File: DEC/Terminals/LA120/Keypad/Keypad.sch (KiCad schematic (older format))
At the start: 23 parts, among them J1 TO KEYBOARD, SW1 ENTER, SW10 9, SW11 0, SW12 COMMA, SW13 MINUS, SW14 PF1, SW15 PF2, SW16 PF3, SW17 PF4, SW18 PERIOD, SW2 1, SW3 2, SW4 3, SW5 4, SW6 5, SW7 6, SW8 7, SW9 8

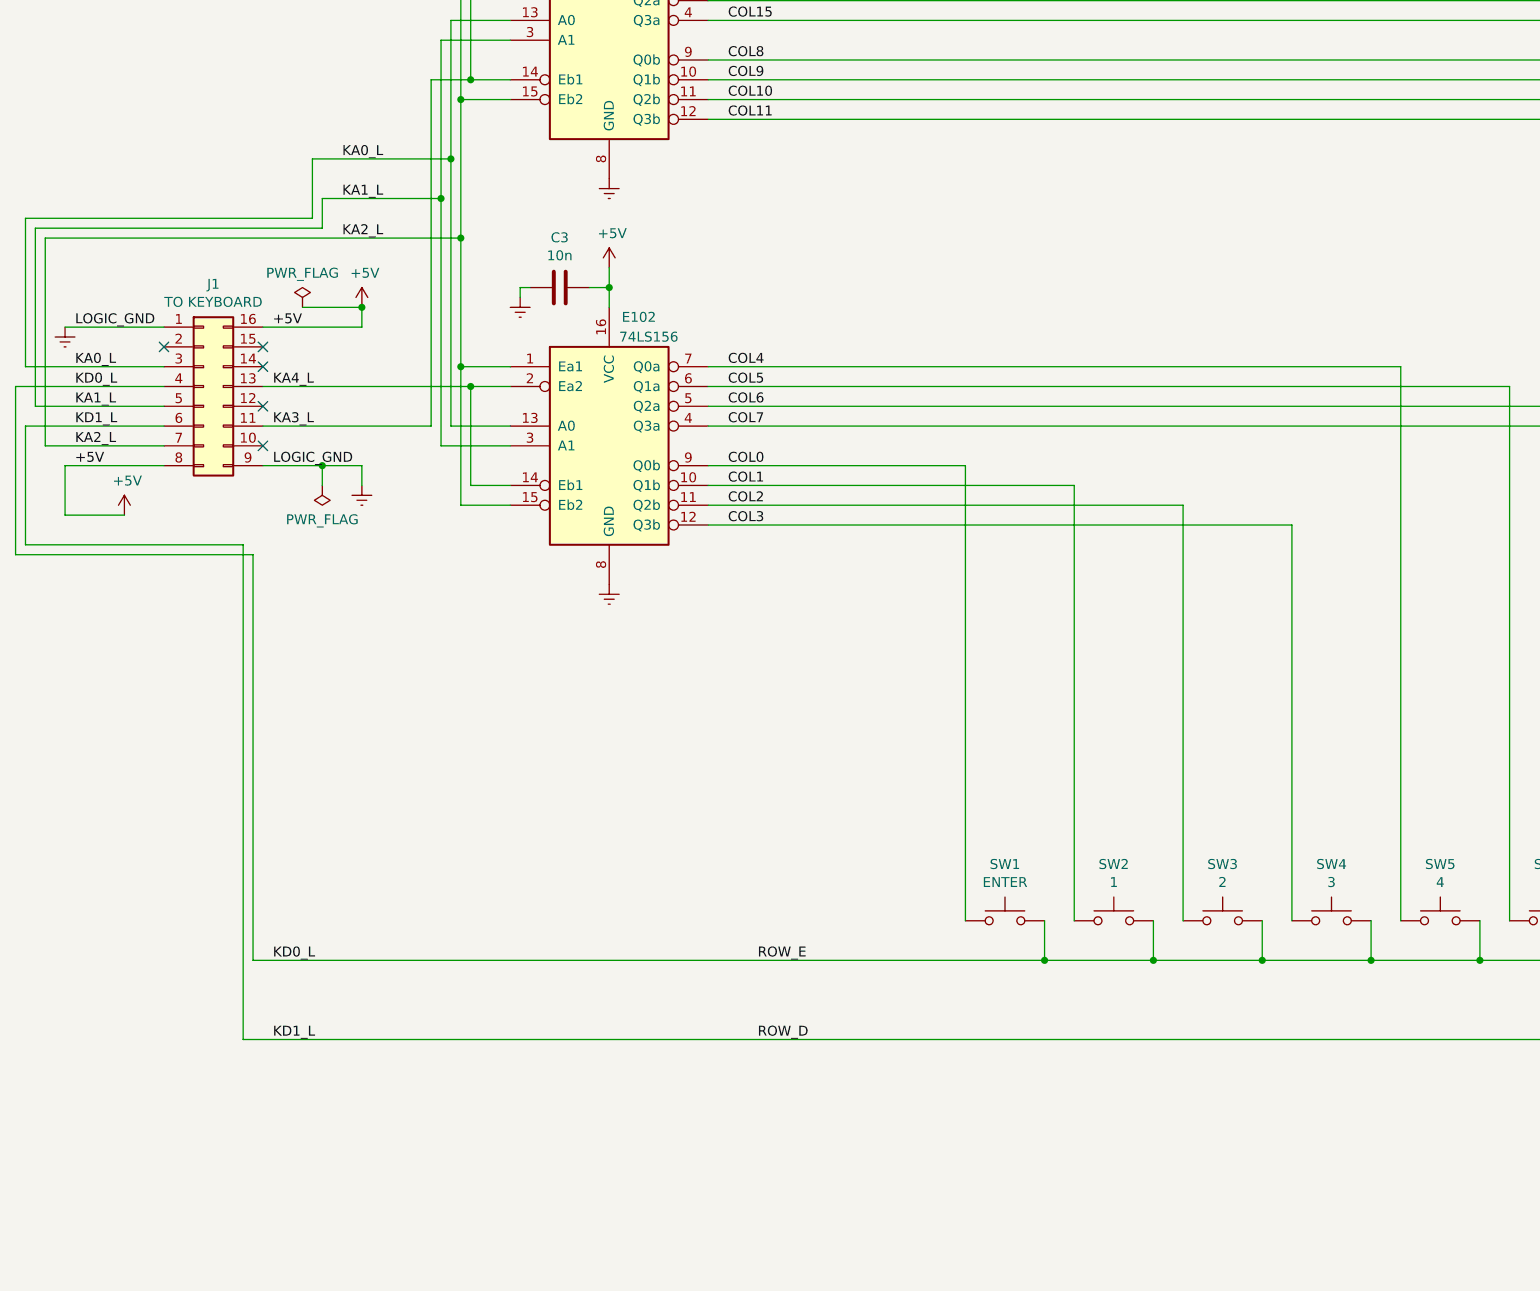
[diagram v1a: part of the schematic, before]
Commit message: Adds DEC LA120 keyboard, keypad, motherboard
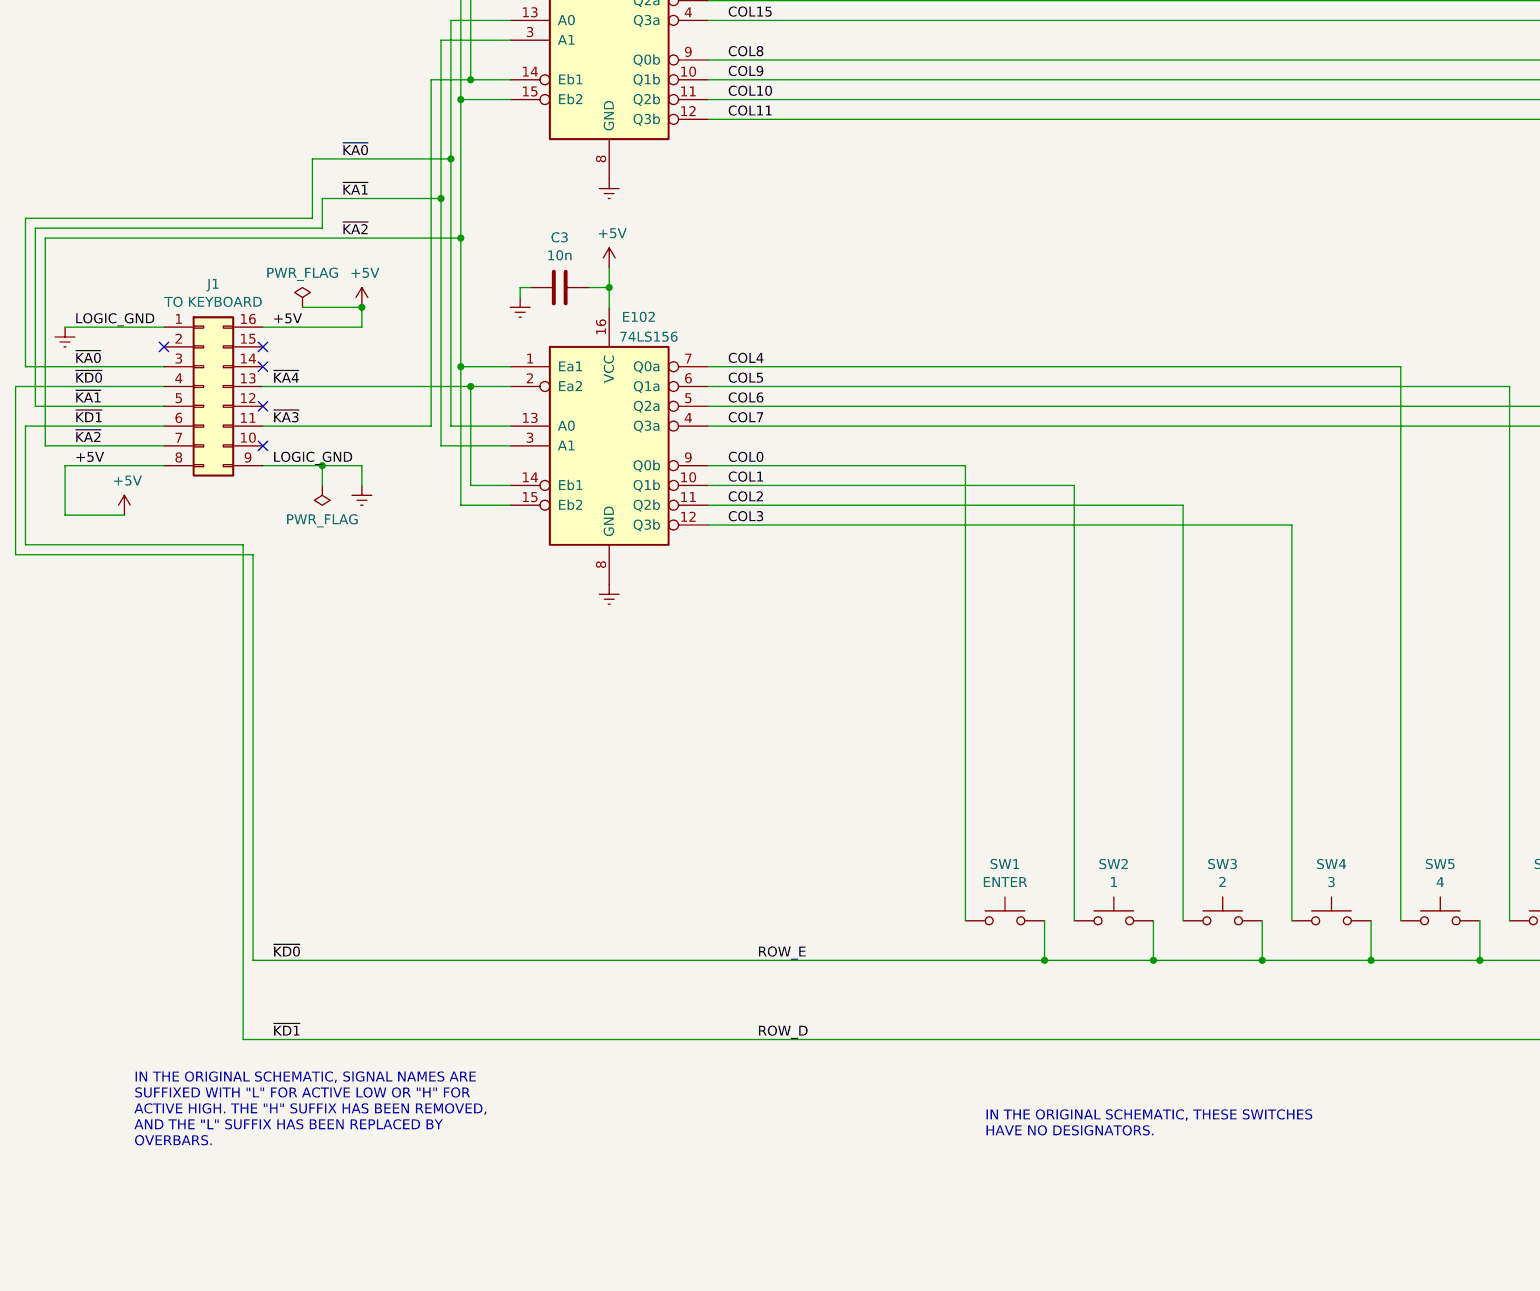
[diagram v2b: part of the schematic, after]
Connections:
- net KA0_L renamed ~KA0
- net KA1_L renamed ~KA1
- net KA2_L renamed ~KA2
- net KA3_L renamed ~KA3
- net KA4_L renamed ~KA4
- net KD0_L renamed ROW_E
- net KD1_L renamed ROW_D
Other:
- note added: "IN THE ORIGINAL SCHEMATIC, SIGNAL NAMES ARE\nSUFFIXED WITH "L" FOR ACTIVE LOW OR "H" FOR\nACTIVE HIGH. THE "H" SUFFIX HAS BEEN REMOVED,\nAND THE "L" SUFFIX HAS BEEN REPLACED BY\nOVERBARS."
- note added: "IN THE ORIGINAL SCHEMATIC, THESE SWITCHES\nHAVE NO DESIGNATORS."
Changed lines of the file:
@@
 $EndComp
 Text Label 2900 3650 0    50   ~ 0
-KA2_L
+~KA2
 Text Label 2900 3450 0    50   ~ 0
-KA1_L
+~KA1
 Text Label 2900 3250 0    50   ~ 0
-KA0_L
+~KA0
 $Comp
 L power:+5V #PWR0101
@@
 Connection ~ 6450 7300
 Text Label 2550 7300 0    50   ~ 0
-KD0_L
+~KD0
 Wire Wire Line
 	2400 7700 12550 7700
@@
 Connection ~ 12550 7700
 Text Label 2550 7700 0    50   ~ 0
-KD1_L
+~KD1
 Wire Wire Line
 	14300 7100 14300 6600
@@
 	2000 4800 1500 4800
 Text Label 1550 4300 0    50   ~ 0
-KA0_L
+~KA0
 Text Label 1550 4400 0    50   ~ 0
-KD0_L
+~KD0
 Text Label 1550 4500 0    50   ~ 0
-KA1_L
+~KA1
 Text Label 1550 4600 0    50   ~ 0
-KD1_L
+~KD1
 Text Label 1550 4700 0    50   ~ 0
-KA2_L
+~KA2
 Wire Wire Line
 	2500 4800 2800 4800
@@
 LOGIC_GND
 Text Label 2550 4600 0    50   ~ 0
-KA3_L
+~KA3
 Text Label 2550 4400 0    50   ~ 0
-KA4_L
+~KA4
 Text Label 2550 4100 0    50   ~ 0
 +5V
@@
 Wire Wire Line
 	1250 4400 2000 4400
+Text Notes 1850 8250 0    50   ~ 0
+IN THE ORIGINAL SCHEMATIC, SIGNAL NAMES ARE\nSUFFIXED WITH "L" FOR ACTIVE LOW OR "H" FOR\nACTIVE HIGH. THE "H" SUFFIX HAS BEEN REMOVED,\nAND THE "L" SUFFIX HAS BEEN REPLACED BY\nOVERBARS.
+Text Notes 6150 8200 0    50   ~ 0
+IN THE ORIGINAL SCHEMATIC, THESE SWITCHES\nHAVE NO DESIGNATORS.
 $EndSCHEMATC
